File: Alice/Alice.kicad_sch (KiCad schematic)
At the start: 0 parts

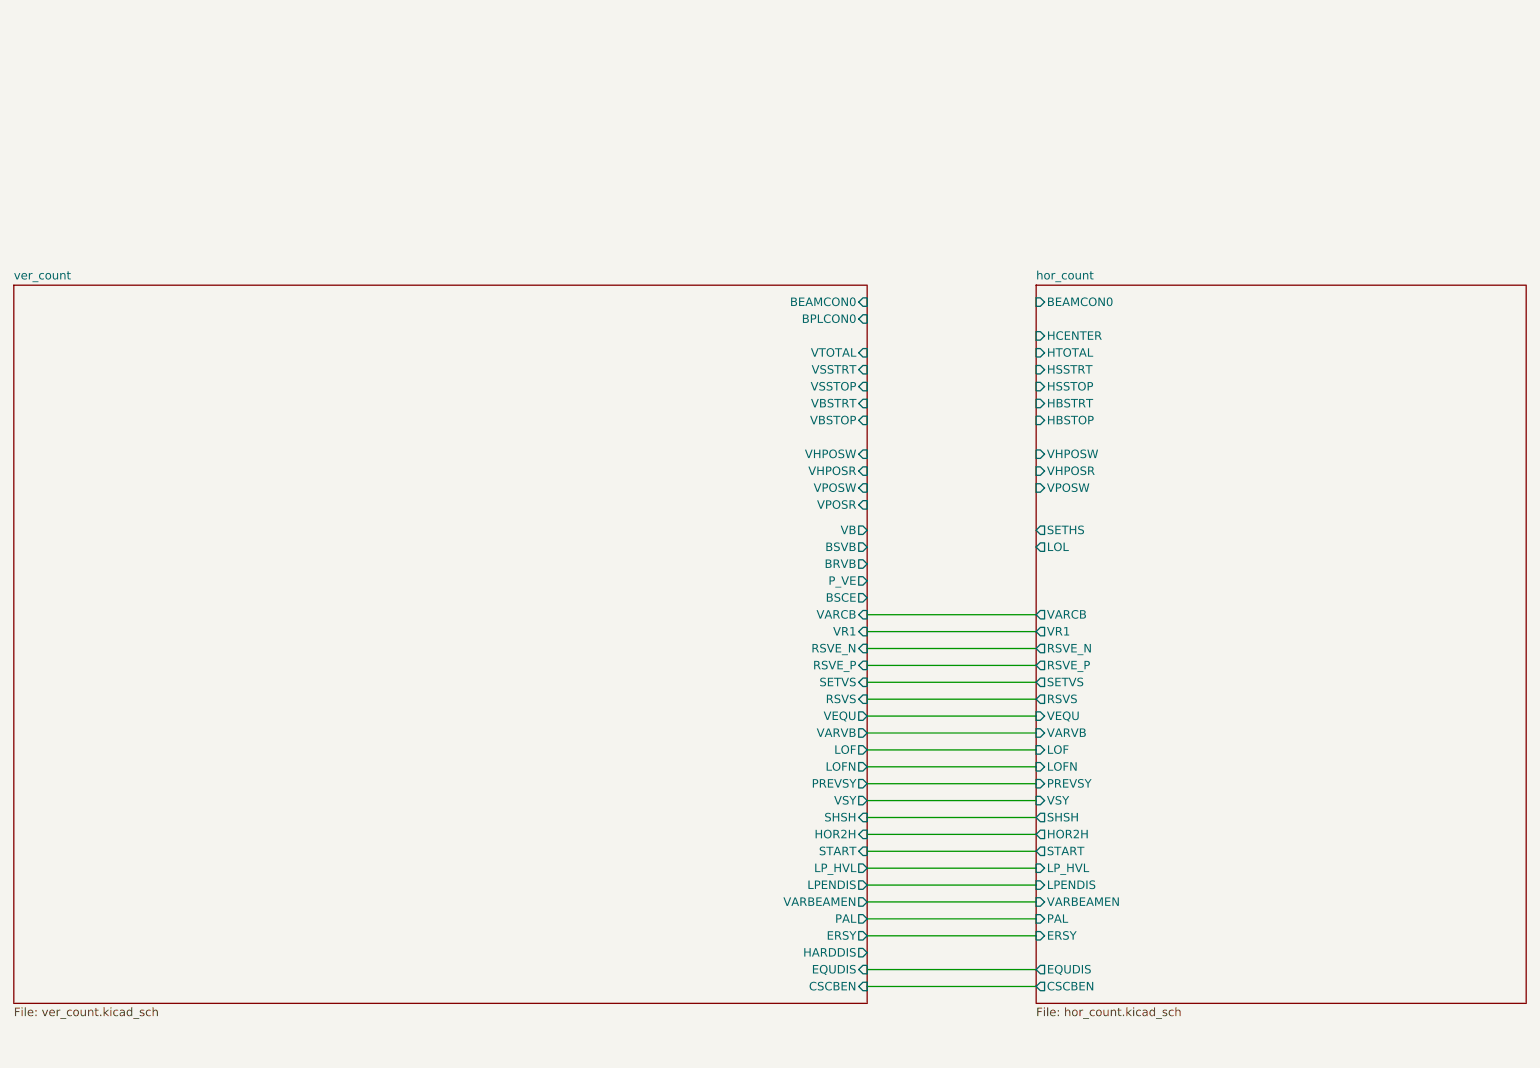
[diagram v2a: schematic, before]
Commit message: Fixed DMA sheet added (partial)
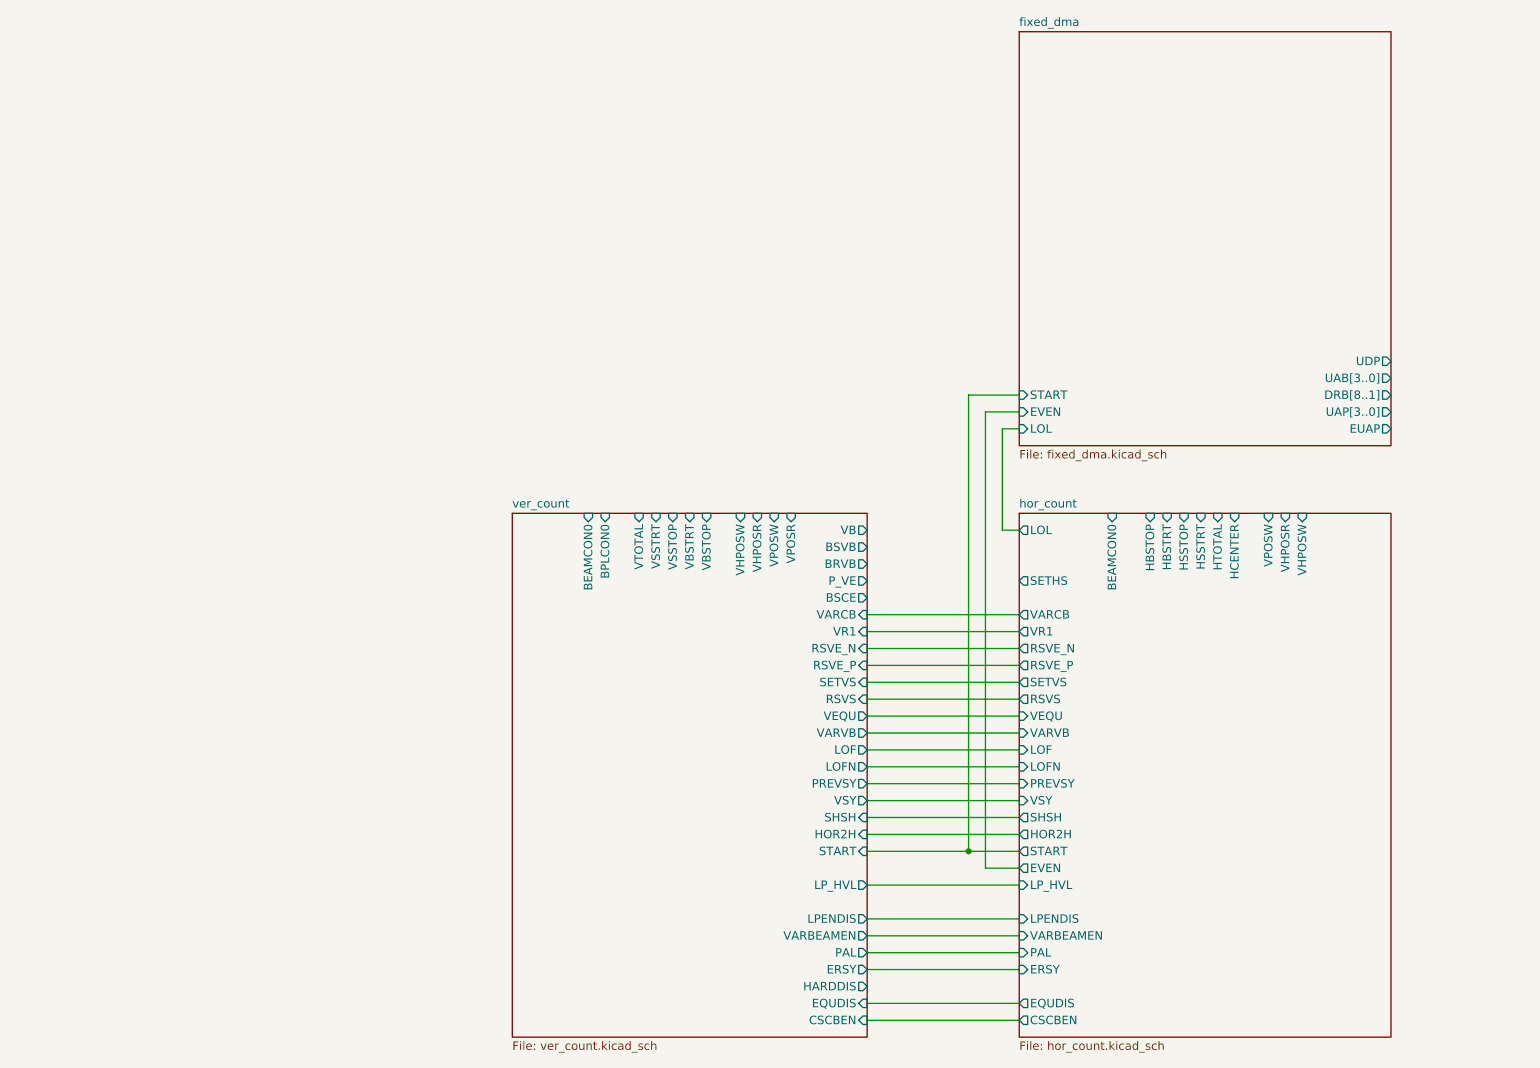
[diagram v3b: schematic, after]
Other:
- added sheet fixed_dma (fixed_dma.kicad_sch)
- sheet hor_count ports: added EVEN; removed none

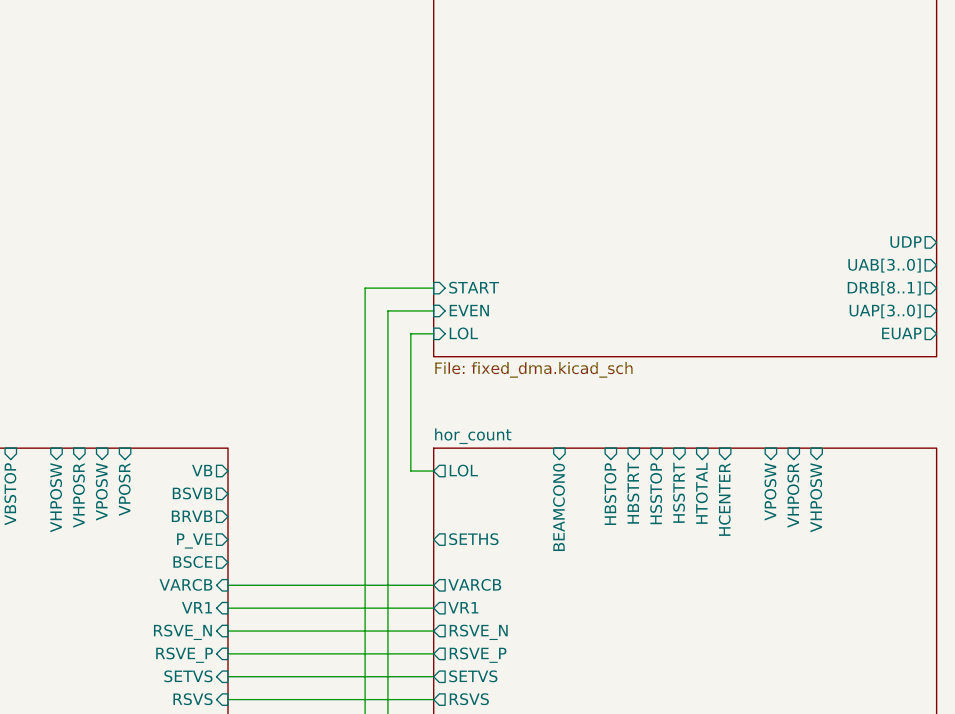
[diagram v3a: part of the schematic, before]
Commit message: Fixed DMA sheet updated
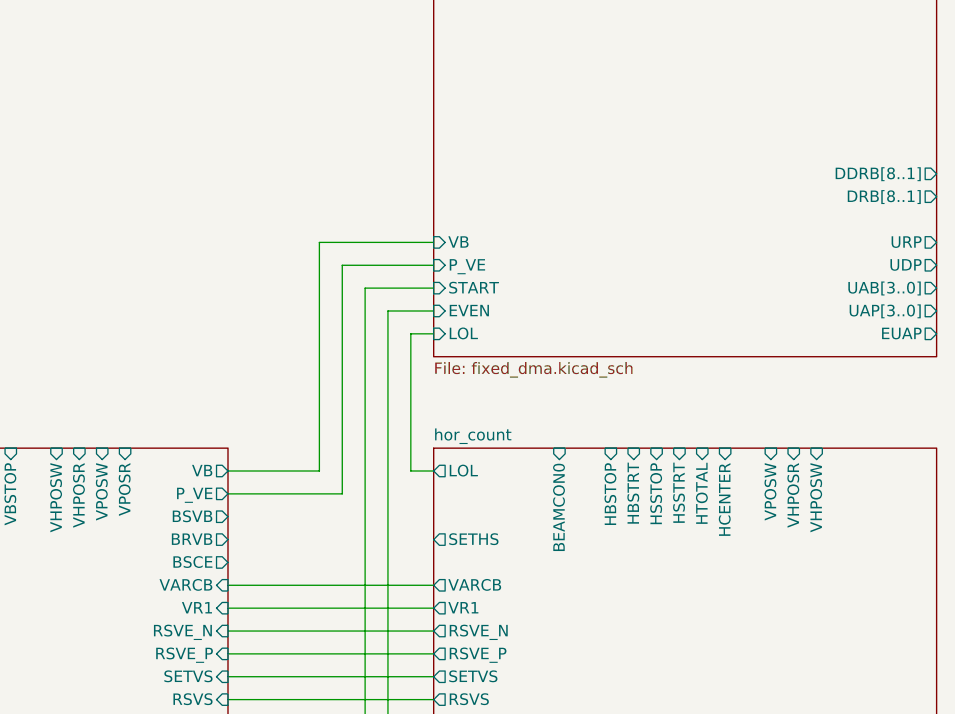
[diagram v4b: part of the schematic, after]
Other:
- sheet fixed_dma ports: added DDRB[8..1], P_VE, URP, VB; removed none
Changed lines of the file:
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@@
+    (stroke (width 0) (type default) (color 0 0 0 0))
+  )
+  (wire (pts (xy 355.6 294.64) (xy 365.76 294.64))
     (stroke (width 0) (type default) (color 0 0 0 0))
   )
@@
     (stroke (width 0) (type default) (color 0 0 0 0))
   )
+  (wire (pts (xy 365.76 269.24) (xy 378.46 269.24))
+    (stroke (width 0) (type default) (color 0 0 0 0))
+  )
   (wire (pts (xy 355.6 368.3) (xy 378.46 368.3))
     (stroke (width 0) (type default) (color 0 0 0 0))
@@
     (stroke (width 0) (type default) (color 0 0 0 0))
   )
+  (wire (pts (xy 378.46 271.78) (xy 368.3 271.78))
+    (stroke (width 0) (type default) (color 0 0 0 0))
+  )
   (wire (pts (xy 355.6 335.28) (xy 378.46 335.28))
     (stroke (width 0) (type default) (color 0 0 0 0))
@@
     (stroke (width 0) (type default) (color 0 0 0 0))
   )
+  (wire (pts (xy 365.76 294.64) (xy 365.76 269.24))
+    (stroke (width 0) (type default) (color 0 0 0 0))
+  )
   (wire (pts (xy 355.6 353.06) (xy 378.46 353.06))
     (stroke (width 0) (type default) (color 0 0 0 0))
   )
+  (wire (pts (xy 368.3 297.18) (xy 355.6 297.18))
+    (stroke (width 0) (type default) (color 0 0 0 0))
+  )
   (wire (pts (xy 373.38 276.86) (xy 373.38 345.44))
     (stroke (width 0) (type default) (color 0 0 0 0))
   )
   (wire (pts (xy 355.6 360.68) (xy 378.46 360.68))
+    (stroke (width 0) (type default) (color 0 0 0 0))
+  )
+  (wire (pts (xy 368.3 271.78) (xy 368.3 297.18))
     (stroke (width 0) (type default) (color 0 0 0 0))
   )
@@
       (effects (font (size 1.27 1.27)) (justify right))
     )
-    (pin "BSVB" output (at 355.6 297.18 0)
+    (pin "BSVB" output (at 355.6 299.72 0)
       (effects (font (size 1.27 1.27)) (justify right))
     )
@@
       (effects (font (size 1.27 1.27)) (justify right))
     )
-    (pin "P_VE" output (at 355.6 302.26 0)
+    (pin "P_VE" output (at 355.6 297.18 0)
       (effects (font (size 1.27 1.27)) (justify right))
     )
@@
       (effects (font (size 1.27 1.27)) (justify right))
     )
-    (pin "BRVB" output (at 355.6 299.72 0)
+    (pin "BRVB" output (at 355.6 302.26 0)
       (effects (font (size 1.27 1.27)) (justify right))
     )
@@
       (effects (font (size 1.27 1.27)) (justify right))
     )
-    (pin "DRB[8..1]" output (at 434.34 274.32 0)
-      (effects (font (size 1.27 1.27)) (justify right))
-    )
-    (pin "UAB[3..0]" output (at 434.34 271.78 0)
-      (effects (font (size 1.27 1.27)) (justify right))
-    )
-    (pin "UDP" output (at 434.34 269.24 0)
+    (pin "DRB[8..1]" output (at 434.34 264.16 0)
+      (effects (font (size 1.27 1.27)) (justify right))
+    )
+    (pin "UAB[3..0]" output (at 434.34 274.32 0)
+      (effects (font (size 1.27 1.27)) (justify right))
+    )
+    (pin "UDP" output (at 434.34 271.78 0)
+      (effects (font (size 1.27 1.27)) (justify right))
+    )
+    (pin "P_VE" input (at 378.46 271.78 180)
+      (effects (font (size 1.27 1.27)) (justify left))
+    )
+    (pin "VB" input (at 378.46 269.24 180)
+      (effects (font (size 1.27 1.27)) (justify left))
+    )
+    (pin "URP" output (at 434.34 269.24 0)
+      (effects (font (size 1.27 1.27)) (justify right))
+    )
+    (pin "DDRB[8..1]" output (at 434.34 261.62 0)
       (effects (font (size 1.27 1.27)) (justify right))
     )
@@
       (reference "AND_43") (unit 1) (value "AND3") (footprint "")
     )
+    (path "/e894cc74-6f5d-406a-b8a9-c5dbe3f8ad47/5ffc5df3-6995-4d07-a3c9-008a21e62bb5"
+      (reference "AND_44") (unit 1) (value "AND2") (footprint "")
+    )
+    (path "/e894cc74-6f5d-406a-b8a9-c5dbe3f8ad47/92ca404e-f495-4eca-b731-543c0ce7bba6"
+      (reference "AND_45") (unit 1) (value "AND2") (footprint "")
+    )
+    (path "/e894cc74-6f5d-406a-b8a9-c5dbe3f8ad47/97093bfe-4c55-4e29-b6c1-802d235158e0"
+      (reference "AND_46") (unit 1) (value "AND2") (footprint "")
+    )
     (path "/d34432c0-ab02-4dab-851f-3fb8163b7223/c6da32e9-082f-42b3-8220-701866caef85"
       (reference "BEAMCON0_LB0") (unit 1) (value "LB2") (footprint "")
@@
       (reference "DMAL_FF3") (unit 1) (value "DFF") (footprint "")
     )
+    (path "/e894cc74-6f5d-406a-b8a9-c5dbe3f8ad47/351fb75b-31b3-4edd-b623-c2632a1f9fba"
+      (reference "DRB_FF1") (unit 1) (value "DFF") (footprint "")
+    )
+    (path "/e894cc74-6f5d-406a-b8a9-c5dbe3f8ad47/944aa0c3-e754-47c3-a8ba-19ffa16b5065"
+      (reference "DRB_FF2") (unit 1) (value "DFF") (footprint "")
+    )
+    (path "/e894cc74-6f5d-406a-b8a9-c5dbe3f8ad47/0140c631-253e-4741-8fd4-7369e67b5ec8"
+      (reference "DRB_FF3") (unit 1) (value "DFF") (footprint "")
+    )
+    (path "/e894cc74-6f5d-406a-b8a9-c5dbe3f8ad47/b7bd03a0-37d8-4756-b4c2-61b959a6a6ad"
+      (reference "DRB_FF4") (unit 1) (value "DFF") (footprint "")
+    )
+    (path "/e894cc74-6f5d-406a-b8a9-c5dbe3f8ad47/deb5c562-ef00-4387-92ed-f3bb7e2c3d3d"
+      (reference "DRB_FF5") (unit 1) (value "DFF") (footprint "")
+    )
+    (path "/e894cc74-6f5d-406a-b8a9-c5dbe3f8ad47/b45f3077-9908-488c-aae4-5e08a0d55dad"
+      (reference "DRB_FF6") (unit 1) (value "DFF") (footprint "")
+    )
+    (path "/e894cc74-6f5d-406a-b8a9-c5dbe3f8ad47/c59ed20a-4dc2-4aa7-beb9-dbf04f5423cd"
+      (reference "DRB_FF7") (unit 1) (value "DFF") (footprint "")
+    )
+    (path "/e894cc74-6f5d-406a-b8a9-c5dbe3f8ad47/c85364ae-313b-42fa-b0a2-3554891737bd"
+      (reference "DRB_FF8") (unit 1) (value "DFF") (footprint "")
+    )
     (path "/d34432c0-ab02-4dab-851f-3fb8163b7223/c436b325-f34b-4f42-b0ac-2e7fff5c3665"
       (reference "HBC_CMP1") (unit 1) (value "CMPD") (footprint "")
@@
       (reference "NOT_17") (unit 1) (value "NOT") (footprint "")
     )
+    (path "/e894cc74-6f5d-406a-b8a9-c5dbe3f8ad47/4242ceb0-fe6f-4337-99f5-b82597deafe6"
+      (reference "NOT_18") (unit 1) (value "NOT") (footprint "")
+    )
     (path "/2741f2f7-0689-47b7-9f91-a147d422d2dd/466ddeb0-f60d-4004-b8f0-c3c6cf3ba62f"
       (reference "OLDVB_SR1") (unit 1) (value "SR") (footprint "")
@@
       (reference "OR_23") (unit 1) (value "OR2") (footprint "")
     )
+    (path "/e894cc74-6f5d-406a-b8a9-c5dbe3f8ad47/158ccae0-9139-475e-97aa-95e06e051332"
+      (reference "OR_24") (unit 1) (value "OR3") (footprint "")
+    )
+    (path "/e894cc74-6f5d-406a-b8a9-c5dbe3f8ad47/70e61d38-04cc-448c-b616-67c753aba481"
+      (reference "OR_25") (unit 1) (value "OR2") (footprint "")
+    )
+    (path "/e894cc74-6f5d-406a-b8a9-c5dbe3f8ad47/1738d35c-5930-4e61-b1b6-6c66476a0967"
+      (reference "OR_26") (unit 1) (value "OR2") (footprint "")
+    )
     (path "/2741f2f7-0689-47b7-9f91-a147d422d2dd/4e0e8806-c1ed-4bfd-a3fc-e8d5ff3e8027"
       (reference "PVE_SR1") (unit 1) (value "SR") (footprint "")
@@
       (reference "Q321") (unit 1) (value "NOT_OC") (footprint "")
     )
+    (path "/e894cc74-6f5d-406a-b8a9-c5dbe3f8ad47/72a3214a-8a21-43f7-a845-5d28ea0cee25"
+      (reference "Q322") (unit 1) (value "NOT_OC") (footprint "")
+    )
+    (path "/e894cc74-6f5d-406a-b8a9-c5dbe3f8ad47/372ec6cc-1a03-4f1d-8b04-41b1e2954c0d"
+      (reference "Q323") (unit 1) (value "NOT_OC") (footprint "")
+    )
+    (path "/e894cc74-6f5d-406a-b8a9-c5dbe3f8ad47/b715e0e7-efa5-4809-a409-4bd899c20865"
+      (reference "Q324") (unit 1) (value "NOT_OC") (footprint "")
+    )
+    (path "/e894cc74-6f5d-406a-b8a9-c5dbe3f8ad47/7c5b382d-fed3-4da2-be63-22c2fe099817"
+      (reference "Q325") (unit 1) (value "NOT_OC") (footprint "")
+    )
+    (path "/e894cc74-6f5d-406a-b8a9-c5dbe3f8ad47/088aff84-6c62-4dcf-a69d-61cc797d74f6"
+      (reference "Q326") (unit 1) (value "NOT_OC") (footprint "")
+    )
+    (path "/e894cc74-6f5d-406a-b8a9-c5dbe3f8ad47/d504d6ad-6b82-4636-923c-a6608d3eb270"
+      (reference "Q327") (unit 1) (value "NOT_OC") (footprint "")
+    )
+    (path "/e894cc74-6f5d-406a-b8a9-c5dbe3f8ad47/0f7b42b3-c84c-44ef-8834-bd9d4a625894"
+      (reference "Q328") (unit 1) (value "NOT_OC") (footprint "")
+    )
+    (path "/e894cc74-6f5d-406a-b8a9-c5dbe3f8ad47/25e45523-8fb1-4f98-a6ae-def142dba6b0"
+      (reference "Q329") (unit 1) (value "NOT_OC") (footprint "")
+    )
+    (path "/e894cc74-6f5d-406a-b8a9-c5dbe3f8ad47/91730108-dc2f-4aaa-a695-ab47c3463cd8"
+      (reference "Q330") (unit 1) (value "NOT_OC") (footprint "")
+    )
+    (path "/e894cc74-6f5d-406a-b8a9-c5dbe3f8ad47/875bbd32-c797-47cd-bdad-696cb8c2dc1f"
+      (reference "Q331") (unit 1) (value "NOT_OC") (footprint "")
+    )
+    (path "/e894cc74-6f5d-406a-b8a9-c5dbe3f8ad47/fa8032f2-5098-49f3-8c08-c7e0eb7f30ff"
+      (reference "Q332") (unit 1) (value "NOT_OC") (footprint "")
+    )
     (path "/d34432c0-ab02-4dab-851f-3fb8163b7223/e21b86e0-9505-4c7e-aa16-0352f582eaf3"
